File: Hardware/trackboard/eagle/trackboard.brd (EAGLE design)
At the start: 160 x 100 mm, 41 parts, among them Q1 BS170, U1 ADNS-3080, X9.00 RESON

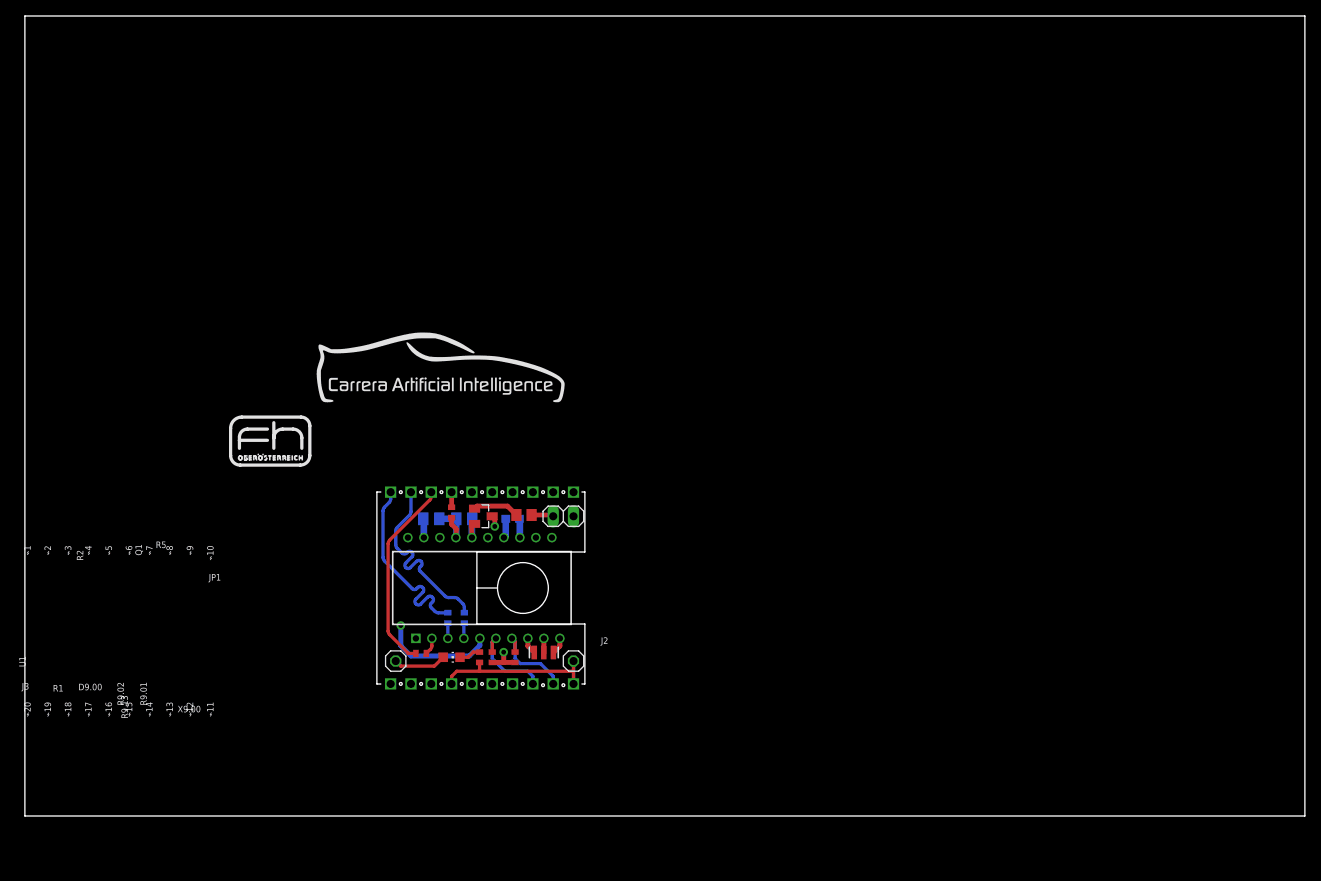
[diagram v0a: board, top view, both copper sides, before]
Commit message: updated trackboard with revised interface
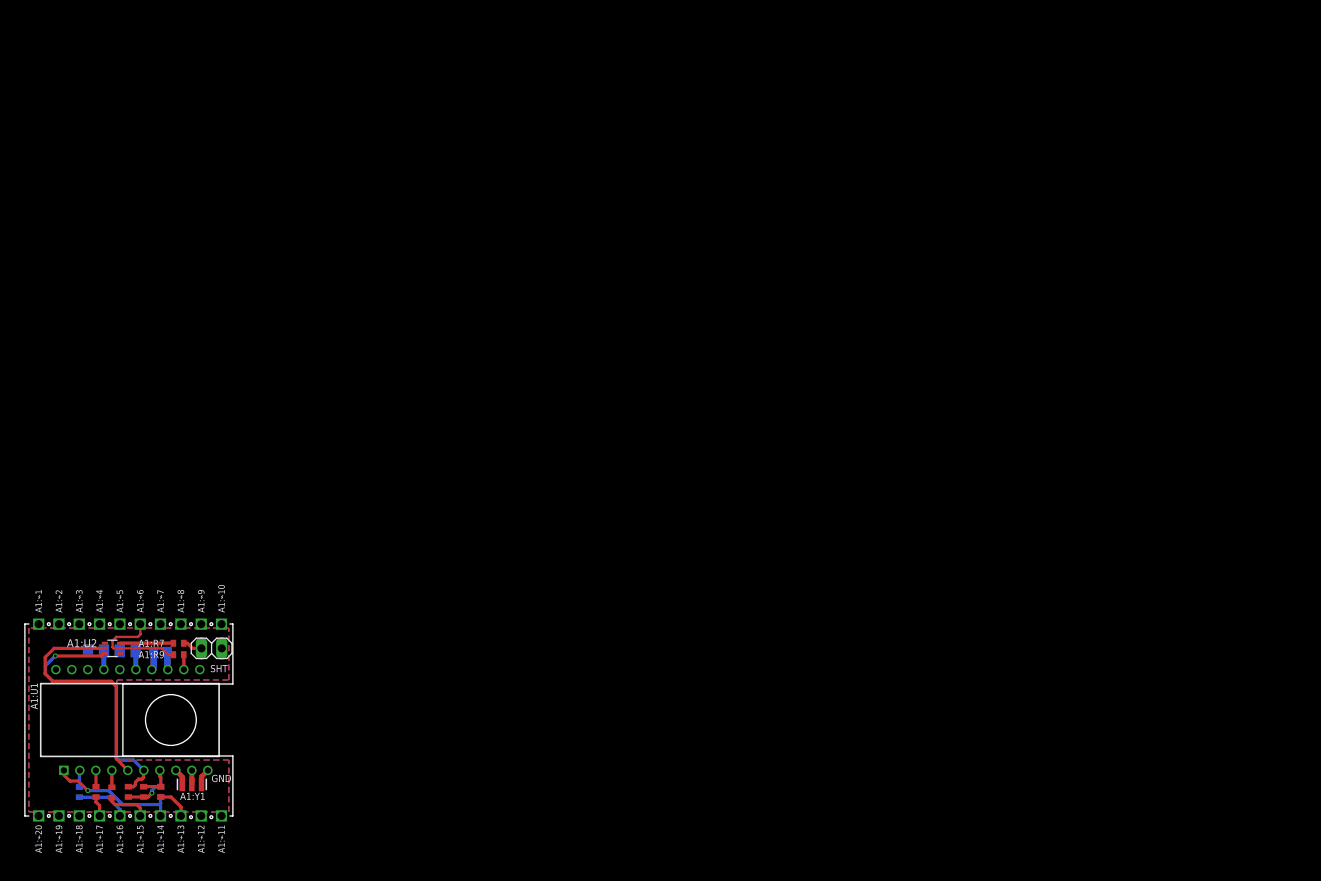
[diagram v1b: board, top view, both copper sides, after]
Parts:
- removed C9.03: 2.2uF, rcl:C1608
- removed C9.04, C9.05: 100nF, rcl:C0805K
- removed D9.00: RED, led:CHIP-LED0805
- removed DCL1: DCL.CARRERAI, kitt.refs:DCL.LOGO-CARRERAI.W30MM
- removed DCL2: DCL.OSH.COPPER'5MM', kitt.refs:DCL.LOGO-OSH.5MM
- removed J2, J3: (no value), pinhead:1X01
- removed JP1: (no value), pinhead:1X02
- removed Q1: BS170, transistor-fet:SOT23
- removed R1, R3, R4: 100R, rcl:R0402
- removed R2, R9.01, R9.02: 10kR, rcl:R0402
- removed R5: (no value), rcl:R0805
- removed R9.13: [PPR], rcl:R0402
- removed REF1: REF.LOGO.UASUA, kitt.refs:REF_LOGO_UASUA
- removed U1: ADNS-3080, kitt.ic:ADNS-3080
- removed X9.00: RESON, Ai_Passives:RESON-SMD
- removed ⌁1, ⌁10, ⌁11, ⌁12, ⌁13, ⌁14, ⌁15, ⌁16, ⌁17, ⌁18, ⌁19, ⌁2, ⌁20, ⌁3, ⌁4, ⌁5, ⌁6, ⌁7, ⌁8, ⌁9: SINGLEPAD40MIL, kitt.con:PAD40MIL
- added A1:C1: 2.2uF/⇤, rcl:C1608
- added A1:C2, A1:C3: 100nF/⇤, rcl:C0805K
- added A1:DCL2: DCL.OSH'3MM-SLK', kitt.refs:DCL.LOGO-OSH.3MM
- added A1:J1: (no value), pinhead:1X02
- added A1:R1, A1:R5, A1:R6, A1:R9: 10kR/⎒, rcl:R0402
- added A1:R2, A1:R3, A1:R4: 100R/⇤, rcl:R0402
- added A1:R7: 200R, rcl:R0402
- added A1:R8: 0R, rcl:R0402
- added A1:U1: ADNS-3080, kitt.ic:ADNS-3080
- added A1:U2: SI1922EDH, kitt.ic:SC70-6
- added A1:Y1: 24MHz, Ai_Passives:RESON-SMD
- added A1:⌁1, A1:⌁10, A1:⌁11, A1:⌁12, A1:⌁13, A1:⌁14, A1:⌁15, A1:⌁16, A1:⌁17, A1:⌁18, A1:⌁19, A1:⌁2, A1:⌁20, A1:⌁3, A1:⌁4, A1:⌁5, A1:⌁6, A1:⌁7, A1:⌁8, A1:⌁9: SINGLEPAD40MIL, kitt.con:PAD40MIL
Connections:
- removed net !CS0: R2.2, U1.1, ⌁4.X
- removed net !CS1: ⌁5.X
- removed net !INT: ⌁6.X
- removed net !PD: R9.01.2, U1.7, ⌁12.X
- removed net +3V3: C9.04.1, C9.05.1, D9.00.A, J3.1, JP1.1, R2.1, R9.01.1, R9.02.1, U1.12, U1.15, U1.17, ⌁10.X
- removed net GND: C9.04.2, C9.05.2, J2.1, Q1.2, R9.13.2, U1.16, U1.19, ⌁11.X, ⌁17.X, ⌁9.X
- removed net GPIO1: ⌁14.X
- removed net GPIO2: ⌁15.X
- removed net GPIO3: ⌁16.X
- removed net MISO: R1.1, ⌁3.X
- removed net MOSI: R4.1, ⌁2.X
- removed net N$1: U1.9, X9.00.2
- removed net N$11: D9.00.C, R9.13.1
- removed net N$2: U1.8, X9.00.3
- removed net N$3: U1.10, X9.00.1
- removed net N$4: Q1.3, U1.5
- removed net N$5: C9.03.1, U1.13
- removed net N$6: C9.03.2, U1.14
- removed net N$7: Q1.1, R5.1
- removed net N$8: JP1.2, R5.2
- removed net N$9: U1.20
- removed net RST: R9.02.2, U1.6, ⌁13.X
- removed net SCL: ⌁8.X
- removed net SCLK: R3.1, ⌁1.X
- removed net SDA: ⌁7.X
- removed net U1.MISO: R1.2, U1.2
- removed net U1.MOSI: R4.2, U1.4
- removed net U1.SCLK: R3.2, U1.3
- removed net V++: ⌁20.X
- new net A1:!CS0: A1:R1.2, A1:U1.1, A1:⌁14.X
- new net A1:!CS1: A1:R8.2, A1:⌁13.X
- new net A1:!INT: A1:⌁20.X
- new net A1:!PD: A1:R6.2, A1:R8.1, A1:U1.7
- new net A1:!RESET: A1:R9.2, A1:U2.5, A1:⌁6.X
- new net A1:+3V3: A1:C2.1, A1:C3.1, A1:J1.1, A1:R1.1, A1:R5.1, A1:R6.1, A1:R9.1, A1:U1.12, A1:U1.15, A1:U1.17, A1:⌁4.X
- new net A1:+5V: A1:⌁5.X
- new net A1:ADC0: A1:⌁9.X
- new net A1:ADC1: A1:⌁8.X
- new net A1:ADC2: A1:⌁7.X
- new net A1:GND: A1:C2.2, A1:C3.2, A1:U1.16, A1:U1.19, A1:U2.1, A1:U2.4, A1:⌁1.X, A1:⌁10.X
- new net A1:LEDCTRL: A1:U1.5, A1:U2.2
- new net A1:MISO: A1:R2.1, A1:⌁16.X
- new net A1:MOSI: A1:R4.1, A1:⌁15.X
- new net A1:MRXS: A1:⌁11.X
- new net A1:MTXS: A1:⌁12.X
- new net A1:N$1: A1:R7.1, A1:U2.6
- new net A1:N$5: A1:C1.1, A1:U1.13
- new net A1:N$6: A1:C1.2, A1:U1.14
- new net A1:N$8: A1:J1.2, A1:R7.2
- new net A1:RST: A1:R5.2, A1:U1.6, A1:U2.3
- new net A1:SCL: A1:⌁19.X
- new net A1:SCLK: A1:R3.1, A1:⌁17.X
- new net A1:SDA: A1:⌁18.X
- new net A1:U1.GUARD: A1:U1.9, A1:Y1.2
- new net A1:U1.MISO: A1:R2.2, A1:U1.2
- new net A1:U1.MOSI: A1:R4.2, A1:U1.4
- new net A1:U1.OSCIN✳: A1:U1.10, A1:Y1.1
- new net A1:U1.OSCOUT✳: A1:U1.8, A1:Y1.3
- new net A1:U1.SCLK: A1:R3.2, A1:U1.3
- new net A1:V++: A1:⌁2.X
- new net A1:VSYS: A1:⌁3.X
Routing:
- net N$4: track 42.5 -> 0.00 mm, vias 2 -> 0
- net A1:RST: track 0.00 -> 35.1 mm, vias 0 -> 1
- net !CS0: track 31.5 -> 0.00 mm
- net A1:LEDCTRL: track 0.00 -> 30.6 mm
- net GND: track 29.9 -> 0.00 mm
- net MISO: track 24.3 -> 0.00 mm
- net SCLK: track 23.8 -> 0.00 mm
- net MOSI: track 23.8 -> 0.00 mm
- net +3V3: track 18.1 -> 0.00 mm, vias 1 -> 0
- net A1:!CS0: track 0.00 -> 16.6 mm, vias 0 -> 1
- net A1:!RESET: track 0.00 -> 13.9 mm
- net RST: track 11.6 -> 0.00 mm
- net A1:+3V3: track 0.00 -> 11.3 mm, vias 0 -> 1
- net !PD: track 11.2 -> 0.00 mm
- net A1:N$1: track 0.00 -> 6.69 mm
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- added copper zone on layer 15, net A1:+3V3
- added copper zone on layer 1, net A1:GND
- added copper zone on layer 16, net A1:GND
- added copper zone on layer 2, net A1:GND
- removed copper zone on layer 15, net +3V3
- removed copper zone on layer 2, net GND
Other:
- board size 160 x 100 mm -> 26 x 24 mm
- board text added: "GND"
- board text added: "HSD'16 CarrerAI"
- board text added: "OSHW SPFMDBC"
- board text added: "P#:KITT-C100'R1"
- board text added: "SHT"
- board text added: "UNIVERSITY OF APPLIED SCIENCE UPPER AUSTRIA"
